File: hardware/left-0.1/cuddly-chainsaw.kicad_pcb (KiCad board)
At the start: 2 copper layers, 3.7 x 3.7 mm, 93 parts, among them J1 USB_C_Receptacle_USB2.0, J2 USB_C_Receptacle_USB2.0, SW1 Encoder_MX_RGB, SW10 MX_RGB, SW11 MX_RGB, SW12 MX_RGB, SW13 MX_RGB, SW14 MX_RGB, SW15 MX_RGB, SW16 MX_RGB, SW17 MX_RGB, SW18 MX_RGB, SW19 MX_RGB, SW2 MX_RGB, SW20 MX_RGB, SW21 MX_RGB, SW22 MX_RGB, SW23 MX_RGB, SW24 MX_RGB, SW25 MX_RGB, SW26 MX_RGB, SW27 MX_RGB, SW28 MX_RGB, SW29 MX_RGB, SW3 MX_RGB, SW30 MX_RGB, SW31 MX_RGB, SW32 MX_RGB, SW33 MX_RGB, SW34 MX_RGB, SW35 SW_Push, SW4 MX_RGB, SW5 MX_RGB, SW6 MX_RGB, SW7 MX_RGB, SW8 MX_RGB, SW9 MX_RGB, U1 USBLC6-2SC6, U2 ATmega32U4-AU, Y1 16MHz

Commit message: first go at board outline done
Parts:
- BZ1, C1, C2, C3, C4, C5, C6, C7, D11, D36, F1, J1, J2, R1, R2, R3, R4, R5, R6, R7, R8, SW35, U1, Y1: moved to B.Cu
- SW10, SW15, SW20: footprint josh-buttons-switches:MX_KEYSWITCH_RGB -> josh-buttons-switches:MX_KEYSWITCH_RGB_1.25U
- SW25: footprint josh-buttons-switches:MX_KEYSWITCH_RGB -> josh-buttons-switches:MX_KEYSWITCH_RGB_2.75U
- SW7: footprint josh-buttons-switches:MX_KEYSWITCH_RGB -> josh-buttons-switches:MX_KEYSWITCH_RGB_1.5U
- SW8: footprint josh-buttons-switches:MX_KEYSWITCH_RGB -> josh-buttons-switches:MX_KEYSWITCH_RGB_1.75U
- SW9: footprint josh-buttons-switches:MX_KEYSWITCH_RGB -> josh-buttons-switches:MX_KEYSWITCH_RGB_2.25U
- U2: value ATmega32U4-AU -> ATmega32U4-MU; footprint Package_QFP:TQFP-44_10x10mm_P0.8mm -> Package_DFN_QFN:QFN-44-1EP_7x7mm_P0.5mm_EP5.2x5.2mm; moved to B.Cu
- moved D36 236.8 mm to (52.3, 103.4)
- moved SW35 236.0 mm to (46.5, 102.1)
- moved R6 235.2 mm to (52.1, 100.9)
- moved C6 233.8 mm to (53.1, 98.6)
- moved R7 233.5 mm to (49.7, 98.2)
- moved Y1 233.0 mm to (45.1, 97.3)
- moved C1 232.6 mm to (53.7, 96.6)
- moved C4 232.2 mm to (50.8, 96.0)
- moved C7 231.2 mm to (47.9, 94.1)
- moved C3 231.1 mm to (50.8, 94.0)
- moved R8 231.0 mm to (44.4, 93.8)
- moved C5 230.1 mm to (47.9, 92.1)
- moved R5 229.7 mm to (44.4, 91.3)
- moved C2 229.1 mm to (47.9, 90.1)
- moved R2 226.6 mm to (55.5, 99.0)
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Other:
- board size 3.7 x 3.7 mm -> 161.9 x 100.8 mm

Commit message: left all connected
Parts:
- added C10: 100n, Capacitor_SMD:C_0603_1608Metric, B.Cu at (237.6, 74.0)
- added C11: 100n, Capacitor_SMD:C_0603_1608Metric, B.Cu at (232.6, 78.0)
- added C12: 100n, Capacitor_SMD:C_0603_1608Metric, B.Cu at (240.1, 70.0)
- added C13: 100n, Capacitor_SMD:C_0603_1608Metric, B.Cu at (240.1, 82.1)
- added C14: 100n, Capacitor_SMD:C_0603_1608Metric, B.Cu at (235.1, 74.0)
- added C15: 100n, Capacitor_SMD:C_0603_1608Metric, B.Cu at (245.6, 70.2)
- added C16: 100n, Capacitor_SMD:C_0603_1608Metric, B.Cu at (245.6, 78.3)
- added C17: 100n, Capacitor_SMD:C_0603_1608Metric, B.Cu at (242.6, 70.0)
- added C18: 100n, Capacitor_SMD:C_0603_1608Metric, B.Cu at (240.0, 78.2)
- added C19: 100n, Capacitor_SMD:C_0603_1608Metric, B.Cu at (245.6, 82.3)
- added C20: 100n, Capacitor_SMD:C_0603_1608Metric, B.Cu at (242.4, 82.2)
- added C21: 100n, Capacitor_SMD:C_0603_1608Metric, B.Cu at (242.5, 78.2)
- added C22: 100n, Capacitor_SMD:C_0603_1608Metric, B.Cu at (232.6, 74.0)
- added C23: 100n, Capacitor_SMD:C_0603_1608Metric, B.Cu at (235.1, 70.0)
- added C24: 100n, Capacitor_SMD:C_0603_1608Metric, B.Cu at (237.6, 70.0)
- added C25: 100n, Capacitor_SMD:C_0603_1608Metric, B.Cu at (242.6, 74.0)
- added C26: 100n, Capacitor_SMD:C_0603_1608Metric, B.Cu at (235.1, 78.0)
- added C27: 100n, Capacitor_SMD:C_0603_1608Metric, B.Cu at (237.6, 78.0)
- added C28: 100n, Capacitor_SMD:C_0603_1608Metric, B.Cu at (240.1, 74.0)
- added C29: 100n, Capacitor_SMD:C_0603_1608Metric, B.Cu at (237.4, 82.0)
- added C8: 100n, Capacitor_SMD:C_0603_1608Metric, B.Cu at (232.6, 70.0)
- added C9: 100n, Capacitor_SMD:C_0603_1608Metric, B.Cu at (245.6, 74.2)
- added D37: WS2812B, LED_SMD:LED_WS2812B_PLCC4_5.0x5.0mm_P3.2mm, B.Cu at (30.4, 66.7)
- added D38: WS2812B, LED_SMD:LED_WS2812B_PLCC4_5.0x5.0mm_P3.2mm, B.Cu at (30.5, 85.7)
- added D39: WS2812B, LED_SMD:LED_WS2812B_PLCC4_5.0x5.0mm_P3.2mm, B.Cu at (30.5, 104.8)
- added D40: WS2812B, LED_SMD:LED_WS2812B_PLCC4_5.0x5.0mm_P3.2mm, B.Cu at (45.5, 118.2)
- added D41: WS2812B, LED_SMD:LED_WS2812B_PLCC4_5.0x5.0mm_P3.2mm, B.Cu at (71.6, 118.1)
- added D42: WS2812B, LED_SMD:LED_WS2812B_PLCC4_5.0x5.0mm_P3.2mm, B.Cu at (95.2, 118.1)
- added D43: WS2812B, LED_SMD:LED_WS2812B_PLCC4_5.0x5.0mm_P3.2mm, B.Cu at (124.2, 118.2)
- added D44: WS2812B, LED_SMD:LED_WS2812B_PLCC4_5.0x5.0mm_P3.2mm, B.Cu at (162.2, 118.1)
- added D45: WS2812B, LED_SMD:LED_WS2812B_PLCC4_5.0x5.0mm_P3.2mm, B.Cu at (169.5, 85.7)
- added D46: WS2812B, LED_SMD:LED_WS2812B_PLCC4_5.0x5.0mm_P3.2mm, B.Cu at (164.9, 47.6)
- added J3: AVR-ISP-6, josh-connectors:AVR_Programmer_SMD, B.Cu at (48.0, 53.5)
- added R9: 22R, Resistor_SMD:R_0603_1608Metric, B.Cu at (67.0, 64.6)
- SW25: footprint josh-buttons-switches:MX_KEYSWITCH_RGB_2.75U -> josh-buttons-switches:MX_KEYSWITCH_RGB_2.75U_REV_STABS
- moved R4 121.6 mm to (160.9, 40.1), turned to 90 degrees
- moved R3 118.1 mm to (162.4, 40.1), turned to 90 degrees
- moved BZ1 73.2 mm to (74.2, 64.6), turned to 0 degrees
- moved D36 62.7 mm to (48.8, 40.8), turned to 180 degrees
- moved R2 61.7 mm to (47.8, 37.8), turned to 90 degrees
- moved R1 58.8 mm to (49.3, 37.8), turned to 90 degrees
- moved U1 58.2 mm to (45.2, 38.2), turned to 270 degrees
- moved F1 55.1 mm to (41.8, 37.1), turned to 90 degrees
- moved D11 54.8 mm to (41.8, 41.1), turned to 90 degrees
- moved R5 49.2 mm to (48.8, 42.3), turned to 180 degrees
- moved SW35 48.3 mm to (52.5, 54.1), turned to 270 degrees
- moved R6 40.7 mm to (52.2, 60.2), turned to 270 degrees
- moved R7 39.5 mm to (46.0, 58.9), turned to 90 degrees
- moved C4 37.2 mm to (47.5, 58.9), turned to 90 degrees
- moved R8 34.9 mm to (44.5, 58.9), turned to 90 degrees
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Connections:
- BZ1 pad 1: (no net) -> Net-(BZ1-Pad1)
- D11 pad 1: (no net) -> +5V
- J1 pad A1: Net-(J1-PadA1) -> GND
- J1 pad A12: Net-(J1-PadA1) -> GND
- J1 pad B1: Net-(J1-PadA1) -> GND
- J1 pad B12: Net-(J1-PadA1) -> GND
- J1 pad S1: Net-(J1-PadA1) -> GND
- SW1 pad 1: (no net) -> /LED_KEYS
- SW1 pad A: (no net) -> /ENC_A
- SW1 pad B: (no net) -> /ENC_B
- SW34 pad 2: (no net) -> /COL_8
- U2 pad 1: (no net) -> /LED_KEYS
- U2 pad 10: (no net) -> /32u4 Microcontroller/PB2
- U2 pad 11: (no net) -> /COL_8
- U2 pad 12: (no net) -> /PIEZO
- U2 pad 20: (no net) -> /ROW_1
- U2 pad 21: (no net) -> /ROW_2
- U2 pad 22: (no net) -> /COL_2
- U2 pad 25: (no net) -> /COL_3
- U2 pad 26: (no net) -> /COL_4
- U2 pad 29: (no net) -> /COL_7
- U2 pad 30: (no net) -> /COL_6
- U2 pad 31: (no net) -> /COL_5
- U2 pad 32: (no net) -> /ROW_5
- U2 pad 36: (no net) -> /COL_1
- U2 pad 37: (no net) -> /ROW_3
- U2 pad 38: (no net) -> /ROW_4
- U2 pad 39: (no net) -> /ENC_A
- U2 pad 40: (no net) -> /ENC_B
- U2 pad 41: (no net) -> /LED_UNDER
- U2 pad 9: (no net) -> /32u4 Microcontroller/PB1
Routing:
- net /COL_7: track 0.00 -> 242.3 mm, vias 0 -> 8
- net /COL_5: track 0.00 -> 213.2 mm, vias 0 -> 2
- net /COL_6: track 0.00 -> 210.9 mm, vias 0 -> 2
- net /ROW_1: track 0.00 -> 173.4 mm, vias 0 -> 2
- net /ROW_4: track 0.00 -> 168.9 mm, vias 0 -> 2
- net /SDA: track 0.00 -> 166.1 mm, vias 0 -> 2
- net /SCL_SERIAL: track 0.00 -> 164.1 mm, vias 0 -> 4
- net /COL_4: track 0.00 -> 161.2 mm, vias 0 -> 2
- net /ROW_2: track 0.00 -> 156.3 mm, vias 0 -> 4
- net /COL_8: track 0.00 -> 155.1 mm, vias 0 -> 5
- net /DAT_1: track 0.00 -> 155.0 mm, vias 0 -> 4
- net /DAT_4: track 0.00 -> 154.1 mm, vias 0 -> 2
- net /DAT_3: track 0.00 -> 153.3 mm, vias 0 -> 2
- net /DAT_2: track 0.00 -> 146.8 mm, vias 0 -> 2
- net /COL_3: track 0.00 -> 142.5 mm, vias 0 -> 2
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- added copper zone on B.Cu, net +5V
- added copper zone on F.Cu, net GND
- added copper zone on B.Cu, net Net-(F1-Pad2)
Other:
- board size 161.9 x 100.8 mm -> 162 x 100.8 mm

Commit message: layout looking nice, just graphics to go
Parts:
- moved C9 212.0 mm to (35.7, 104.0)
- moved C20 205.0 mm to (41.0, 44.1), turned to 180 degrees
- moved C14 200.2 mm to (35.0, 67.3)
- moved C11 196.7 mm to (36.0, 85.0)
- moved C24 192.6 mm to (51.0, 117.5)
- moved C8 182.6 mm to (50.0, 71.1), turned to 0 degrees
- moved C25 179.9 mm to (64.6, 100.0)
- moved C29 170.3 mm to (71.7, 42.9)
- moved C10 166.4 mm to (76.9, 117.3)
- moved C26 155.0 mm to (80.9, 62.0)
- moved C18 154.0 mm to (86.0, 81.0)
- moved C12 146.1 mm to (102.5, 119.0)
- moved C19 141.6 mm to (109.5, 42.9)
- moved C17 131.6 mm to (114.5, 100.0)
- moved C16 121.7 mm to (124.0, 81.0)
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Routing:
- net GND: track 103.5 -> 118.0 mm, vias 66 -> 88
- net +5V: track 34.7 -> 42.3 mm
- net /DAT_1: track 155.0 -> 161.0 mm
- net /SCL_SERIAL: track 164.1 -> 167.9 mm
- net /COL_8: track 155.1 -> 158.1 mm
- net Net-(SW4-Pad4): track 45.7 -> 48.4 mm
- net /ROW_3: track 140.3 -> 138.1 mm
- net /32u4 Microcontroller/nRST: track 16.5 -> 14.4 mm
- net /DAT_3: track 153.3 -> 155.3 mm
- net /COL_4: track 161.2 -> 162.8 mm
- net /COL_5: track 213.2 -> 211.9 mm
- net /DAT_2: track 146.8 -> 145.5 mm
- net /SDA: track 166.1 -> 167.4 mm
- net /COL_7: track 242.3 -> 241.2 mm
- net Net-(D26-Pad2): track 27.3 -> 28.4 mm
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
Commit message: layout ++
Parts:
- added REF**: MountingHole_3.7mm, MountingHole:MountingHole_3.7mm, F.Cu at (66.7, 46.4)
- added REF**: MountingHole_3.7mm, MountingHole:MountingHole_3.7mm, F.Cu at (56.0, 97.0)
- added REF**: MountingHole_3.7mm, MountingHole:MountingHole_3.7mm, F.Cu at (147.5, 102.5)
- added REF**: MountingHole_3.7mm, MountingHole:MountingHole_3.7mm, F.Cu at (142.8, 47.0)
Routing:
- net Net-(SW4-Pad4): track 48.4 -> 51.8 mm
- net /COL_7: track 241.2 -> 243.8 mm

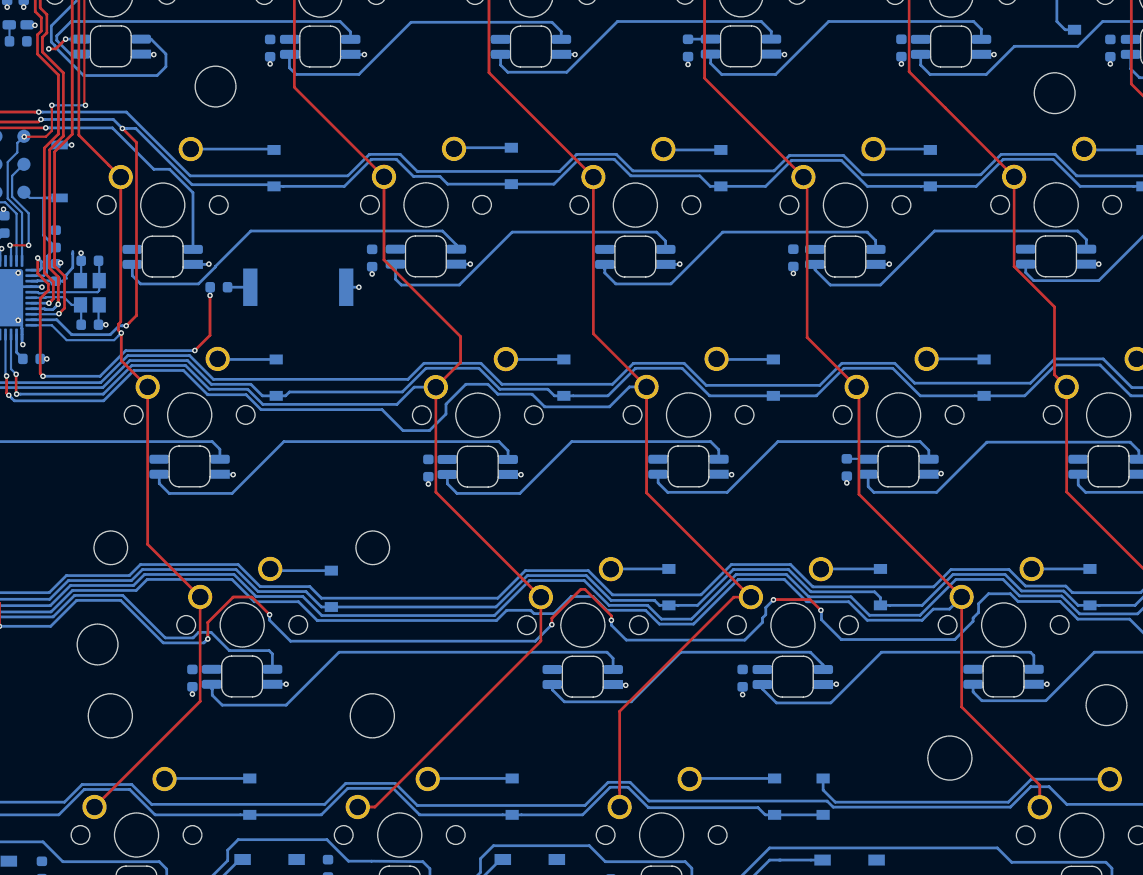
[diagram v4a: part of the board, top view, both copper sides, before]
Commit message: moved mounting oles
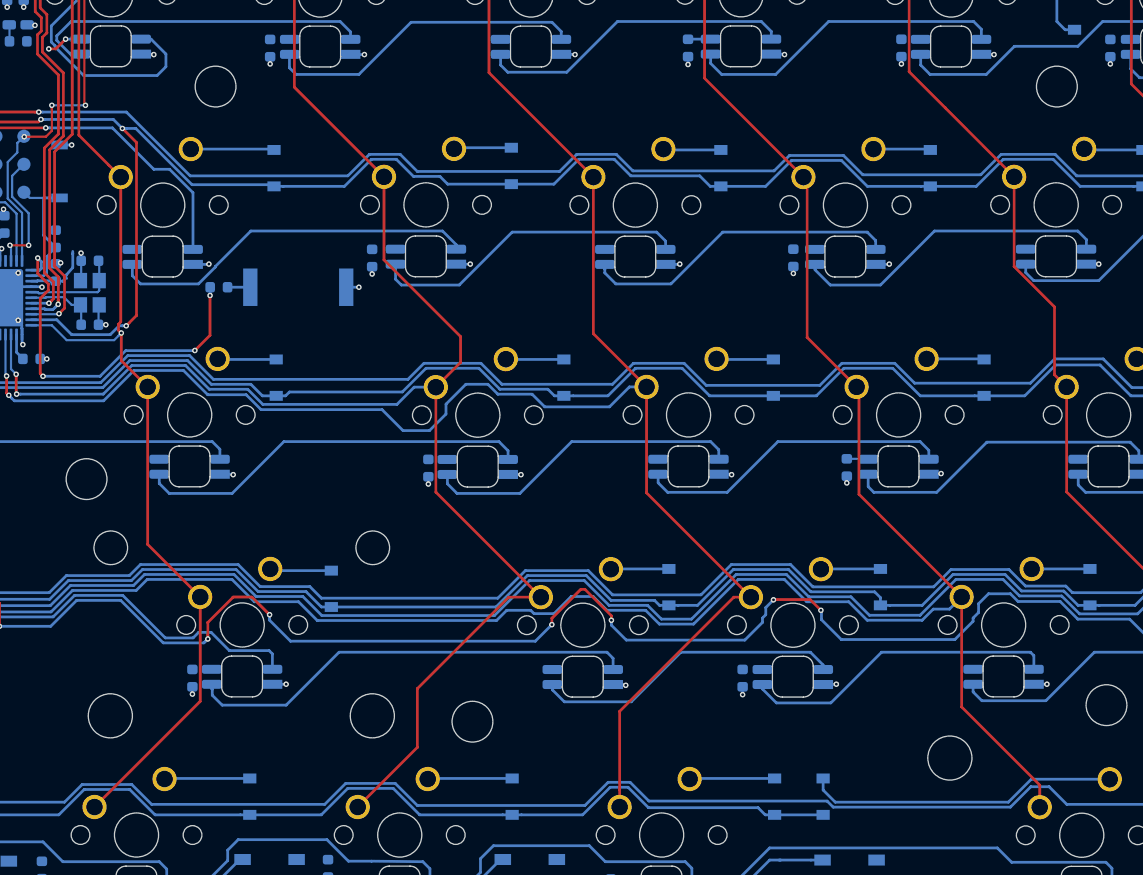
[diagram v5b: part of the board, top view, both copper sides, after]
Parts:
- removed the REF** at (66.7, 46.4)
- added REF**: MountingHole_3.7mm, MountingHole:MountingHole_3.7mm, F.Cu at (90.0, 104.0)
- added REF**: MountingHole_3.7mm, MountingHole:MountingHole_3.7mm, F.Cu at (143.0, 46.4)
- moved REF** 76.1 mm to (66.7, 46.4)
- moved REF** 15.0 mm to (55.0, 82.0)
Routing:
- net /COL_3: track 142.5 -> 143.3 mm
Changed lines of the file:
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@@
     (tracks 1825)
     (zones 0)
-    (modules 131)
+    (modules 132)
     (nets 118)
   )
@@
   )
   (module MountingHole:MountingHole_3.7mm (layer F.Cu)
-    (at 66.7 46.4)
+    (at 90 104)
     (descr "Mounting Hole 3.7mm, no annular")
     (tags "mounting hole 3.7mm no annular")
@@
   )
   (module MountingHole:MountingHole_3.7mm (layer F.Cu)
-    (at 56 97)
+    (at 143 46.4)
+    (descr "Mounting Hole 3.7mm, no annular")
+    (tags "mounting hole 3.7mm no annular")
+    (attr virtual)
+    (fp_text reference REF** (at 0 -4.7) (layer F.SilkS) hide
+      (effects (font (size 1 1) (thickness 0.15)))
+    )
+    (fp_text value MountingHole_3.7mm (at 0 4.7) (layer F.Fab)
+      (effects (font (size 1 1) (thickness 0.15)))
+    )
+    (fp_text user %R (at 0.3 0) (layer F.Fab) hide
+      (effects (font (size 1 1) (thickness 0.15)))
+    )
+    (fp_circle (center 0 0) (end 3.7 0) (layer Cmts.User) (width 0.15))
+    (fp_circle (center 0 0) (end 3.95 0) (layer F.CrtYd) (width 0.05))
+    (pad 1 np_thru_hole circle (at 0 0) (size 3.7 3.7) (drill 3.7) (layers *.Cu *.Mask))
+  )
+  (module MountingHole:MountingHole_3.7mm (layer F.Cu)
+    (at 55 82)
     (descr "Mounting Hole 3.7mm, no annular")
     (tags "mounting hole 3.7mm no annular")
@@
   )
   (module MountingHole:MountingHole_3.7mm (layer F.Cu)
-    (at 142.8 47)
+    (at 66.7 46.4)
     (descr "Mounting Hole 3.7mm, no annular")
     (tags "mounting hole 3.7mm no annular")
@@
   (segment (start 73.4 43.52) (end 73.44 43.48) (width 0.25) (layer B.Cu) (net 76))
   (segment (start 84.43001 40.56999) (end 79.7 45.3) (width 0.25) (layer B.Cu) (net 76))
-  (segment (start 96.2025 96.686884) (end 96.2025 94.265634) (width 0.25) (layer F.Cu) (net 77))
-  (segment (start 96.2025 94.265634) (end 96.2025 92.71) (width 0.25) (layer F.Cu) (net 77))
-  (segment (start 81.149384 111.74) (end 96.2025 96.686884) (width 0.25) (layer F.Cu) (net 77))
-  (segment (start 79.59375 111.74) (end 81.149384 111.74) (width 0.25) (layer F.Cu) (net 77))
   (segment (start 86.6775 83.185) (end 86.6775 73.66) (width 0.25) (layer F.Cu) (net 77))
   (segment (start 96.2025 92.71) (end 86.6775 83.185) (width 0.25) (layer F.Cu) (net 77))
@@
   (segment (start 49.010147 74.293406) (end 48.656594 74.293406) (width 0.25) (layer B.Cu) (net 77))
   (segment (start 84.712821 73.66) (end 83.14782 75.225001) (width 0.25) (layer B.Cu) (net 77))
+  (segment (start 93.29 92.71) (end 96.2025 92.71) (width 0.25) (layer F.Cu) (net 77))
+  (segment (start 79.59375 111.74) (end 85 106.33375) (width 0.25) (layer F.Cu) (net 77))
+  (segment (start 85 101) (end 93.29 92.71) (width 0.25) (layer F.Cu) (net 77))
+  (segment (start 85 106.33375) (end 85 101) (width 0.25) (layer F.Cu) (net 77))
   (segment (start 107.515 60.415) (end 107.515 61.17) (width 0.25) (layer B.Cu) (net 78))
   (segment (start 106.7 59.6) (end 107.515 60.415) (width 0.25) (layer B.Cu) (net 78))

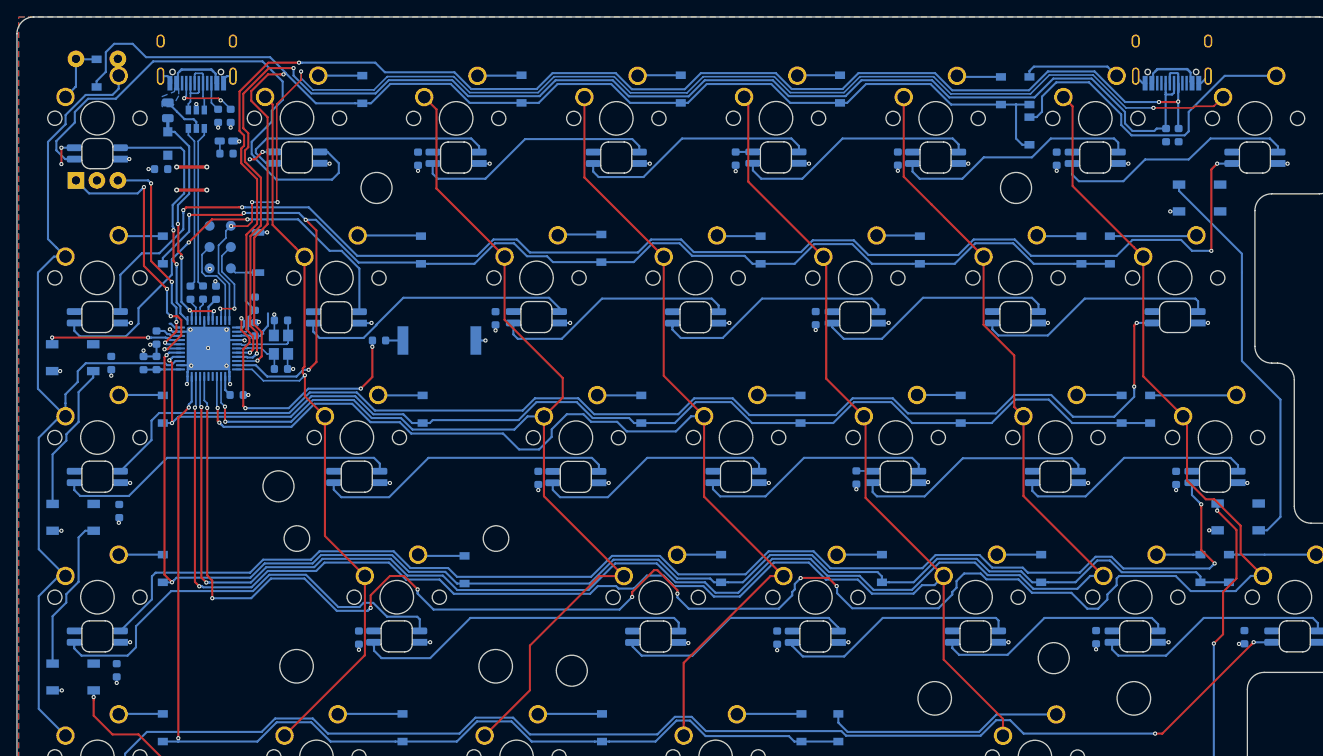
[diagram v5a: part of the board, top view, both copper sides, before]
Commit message: updated components due to jlk change
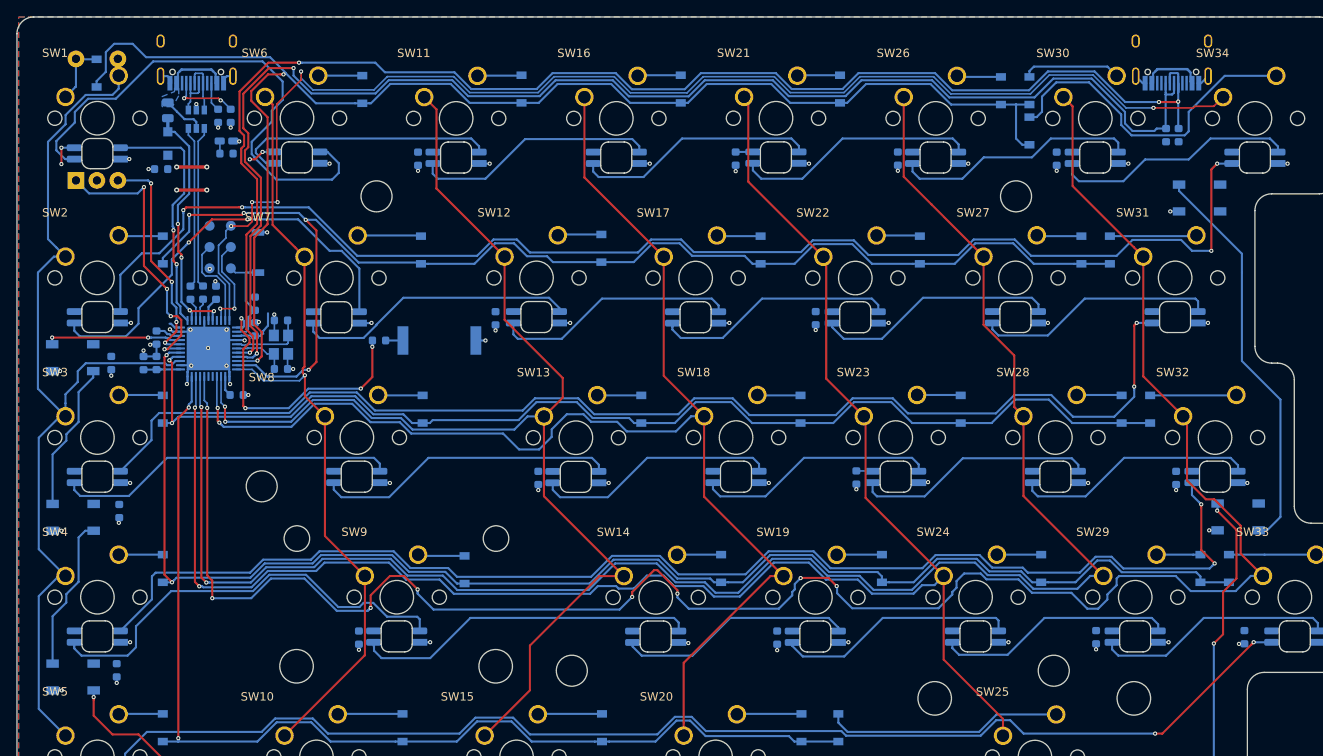
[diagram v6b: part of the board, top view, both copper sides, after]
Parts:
- removed the REF** at (143.0, 46.4)
- removed the REF** at (66.7, 46.4)
- added REF**: MountingHole_3.7mm, MountingHole:MountingHole_3.7mm, F.Cu at (143.0, 47.4)
- added REF**: MountingHole_3.7mm, MountingHole:MountingHole_3.7mm, F.Cu at (66.7, 47.4)
- J3: footprint josh-connectors:AVR_Programmer_SMD -> josh-connectors:AVR_PROG_2.54_SMT
- SW1: footprint josh-buttons-switches:MX_KEYSWITCH_ENCODER_RGB -> josh-keyboard:MX_KEYSWITCH_ENCODER_RGB
- SW10, SW15, SW20: footprint josh-buttons-switches:MX_KEYSWITCH_RGB_1.25U -> josh-keyboard:MX_KEYSWITCH_RGB_1.25U
- SW11, SW12, SW13, SW14, SW16, SW17, SW18, SW19, SW2, SW21, SW22, SW23, SW24, SW26, SW27, SW28, SW29, SW3, SW30, SW31, SW32, SW33, SW34, SW4, SW5, SW6: footprint josh-buttons-switches:MX_KEYSWITCH_RGB -> josh-keyboard:MX_KEYSWITCH_RGB
- SW25: footprint josh-buttons-switches:MX_KEYSWITCH_RGB_2.75U_REV_STABS -> josh-keyboard:MX_KEYSWITCH_RGB_2.75U_REV_STABS
- SW35: footprint josh-buttons-switches:BT_Small_2_Pin -> josh-buttons-switches:SW_Push_PTS820
- SW7: footprint josh-buttons-switches:MX_KEYSWITCH_RGB_1.5U -> josh-keyboard:MX_KEYSWITCH_RGB_1.5U
- SW8: footprint josh-buttons-switches:MX_KEYSWITCH_RGB_1.75U -> josh-keyboard:MX_KEYSWITCH_RGB_1.75U
- SW9: footprint josh-buttons-switches:MX_KEYSWITCH_RGB_2.25U -> josh-keyboard:MX_KEYSWITCH_RGB_2.25U
- moved REF** 2.00 mm to (53.0, 82.0)
- moved REF** 1.50 mm to (147.5, 104.0)
